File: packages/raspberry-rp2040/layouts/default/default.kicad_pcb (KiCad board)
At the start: 4 copper layers, 28 parts

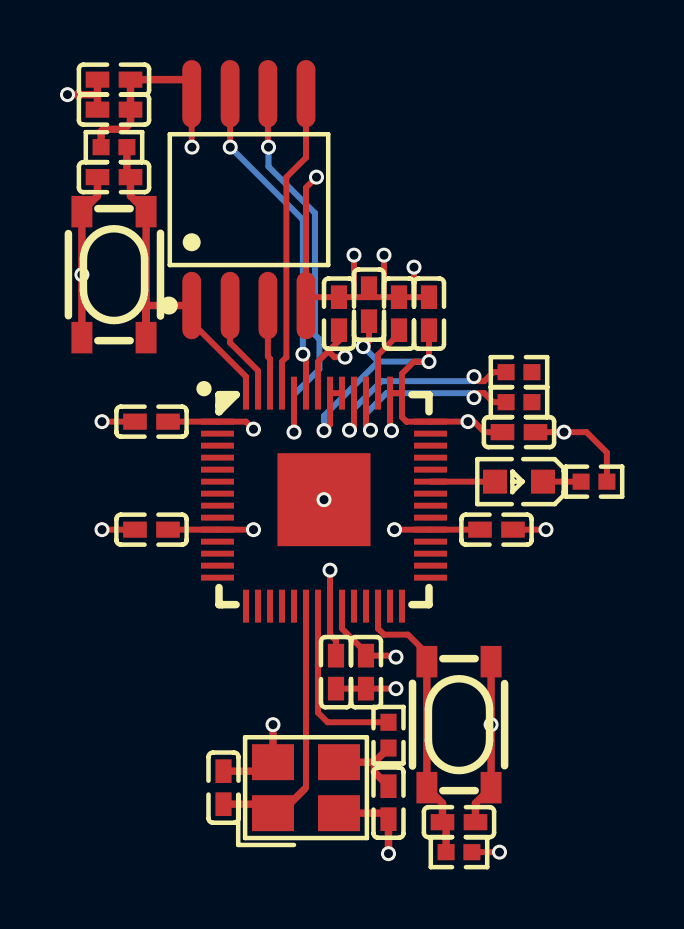
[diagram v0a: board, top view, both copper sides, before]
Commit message: fix docstrings, rename example > usage
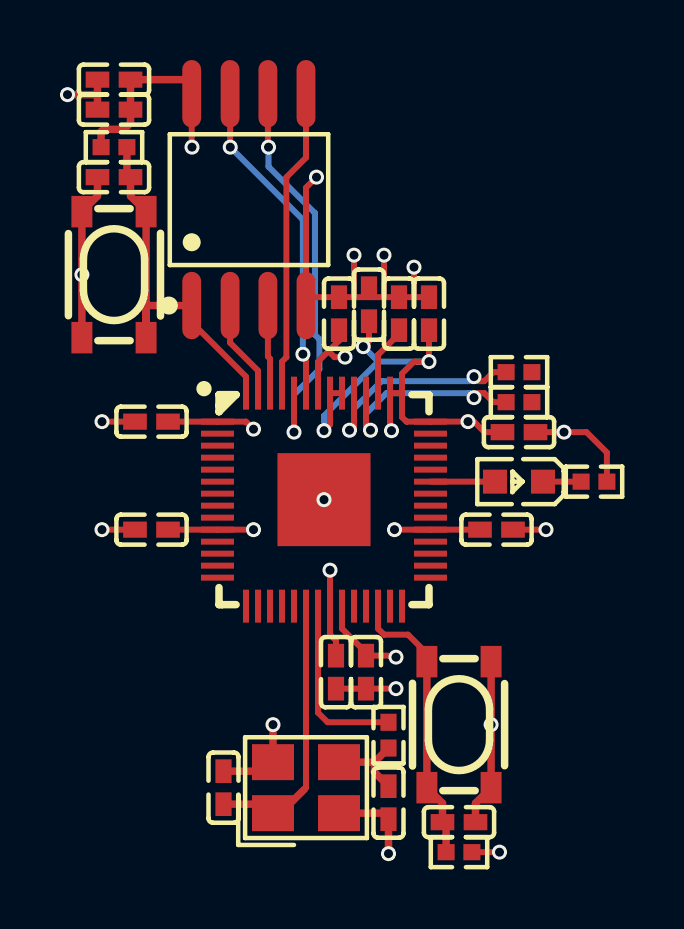
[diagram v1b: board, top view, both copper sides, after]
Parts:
- C5, C6: footprint YAGEO_CC0402JRNPO9BN150:C0402 -> FH_0402CG150J500NT:C0402
- R5, R6: footprint YAGEO_RC0402FR_0727RL:R0402 -> UNI_ROYAL_0402WGF270JTCE:R0402

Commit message: update regulator dependency
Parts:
- R5, R6: footprint UNI_ROYAL_0402WGF270JTCE:R0402 -> YAGEO_RC0402FR_0727RL:R0402
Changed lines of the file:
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@@
         )
     )
-    (footprint "UNI_ROYAL_0402WGF270JTCE:R0402"
+    (footprint "YAGEO_RC0402FR_0727RL:R0402"
         (layer "F.Cu")
         (at 6.5 -4.25 180)
@@
             )
         )
-        (property "Datasheet" "https://www.lcsc.com/datasheet/lcsc_datasheet_2205311900_UNI-ROYAL-Uniroyal-Elec-0402WGF270JTCE_C25100.pdf"
+        (property "Datasheet" "https://www.lcsc.com/datasheet/lcsc_datasheet_2304140030_YAGEO-RC0402FR-0727RL_C138021.pdf"
             (at 0 0 0)
             (layer "User.9")
@@
             )
         )
-        (property "checksum" "f5688ad61e98ad9a0b11cf3927eeb041cb72238f21c6b37db6cf4fe631cbd23f"
+        (property "checksum" "835ff2262c0c781dd32e754197fe87f02981eb4bce2fd6a49a20fee081a98441"
             (at 0 0 0)
             (layer "User.9")
@@
             )
         )
-        (property "__atopile_lib_fp_hash__" "3950a241-3b4c-5b6c-8f80-3fc849177d89"
+        (property "__atopile_lib_fp_hash__" "eb411b3a-b808-da41-e3c1-b5f79249ece2"
             (at 0 0 0)
             (layer "User.9")
@@
             )
         )
-        (property "LCSC" "C25100"
+        (property "LCSC" "C138021"
             (at 0 0 0)
             (layer "User.9")
@@
             )
         )
-        (property "Manufacturer" "UNI-ROYAL(Uniroyal Elec)"
+        (property "Manufacturer" "YAGEO"
             (at 0 0 0)
             (layer "User.9")
@@
             )
         )
-        (property "Partnumber" "0402WGF270JTCE"
+        (property "Partnumber" "RC0402FR-0727RL"
             (at 0 0 0)
             (layer "User.9")
@@
             (net 3 "USB_P")
         )
-        (model "${KIPRJMOD}/../../parts/UNI_ROYAL_0402WGF270JTCE/R0402_L1.0-W0.5-H0.4.step"
+        (model "${KIPRJMOD}/../../parts/YAGEO_RC0402FR_0727RL/R0402_L1.0-W0.5-H0.4.step"
             (offset
                 (xyz 0 0 0)
@@
         )
     )
-    (footprint "UNI_ROYAL_0402WGF270JTCE:R0402"
+    (footprint "YAGEO_RC0402FR_0727RL:R0402"
         (layer "F.Cu")
         (at 6.5 -3.25 180)
@@
             )
         )
-        (property "Datasheet" "https://www.lcsc.com/datasheet/lcsc_datasheet_2205311900_UNI-ROYAL-Uniroyal-Elec-0402WGF270JTCE_C25100.pdf"
+        (property "Datasheet" "https://www.lcsc.com/datasheet/lcsc_datasheet_2304140030_YAGEO-RC0402FR-0727RL_C138021.pdf"
             (at 0 0 0)
             (layer "User.9")
@@
             )
         )
-        (property "checksum" "f5688ad61e98ad9a0b11cf3927eeb041cb72238f21c6b37db6cf4fe631cbd23f"
+        (property "checksum" "835ff2262c0c781dd32e754197fe87f02981eb4bce2fd6a49a20fee081a98441"
             (at 0 0 0)
             (layer "User.9")
@@
             )
         )
-        (property "__atopile_lib_fp_hash__" "3950a241-3b4c-5b6c-8f80-3fc849177d89"
+        (property "__atopile_lib_fp_hash__" "eb411b3a-b808-da41-e3c1-b5f79249ece2"
             (at 0 0 0)
             (layer "User.9")
@@
             )
         )
-        (property "LCSC" "C25100"
+        (property "LCSC" "C138021"
             (at 0 0 0)
             (layer "User.9")
@@
             )
         )
-        (property "Manufacturer" "UNI-ROYAL(Uniroyal Elec)"
+        (property "Manufacturer" "YAGEO"
             (at 0 0 0)
             (layer "User.9")
@@
             )
         )
-        (property "Partnumber" "0402WGF270JTCE"
+        (property "Partnumber" "RC0402FR-0727RL"
             (at 0 0 0)
             (layer "User.9")
@@
             (net 6 "USB_N")
         )
-        (model "${KIPRJMOD}/../../parts/UNI_ROYAL_0402WGF270JTCE/R0402_L1.0-W0.5-H0.4.step"
+        (model "${KIPRJMOD}/../../parts/YAGEO_RC0402FR_0727RL/R0402_L1.0-W0.5-H0.4.step"
             (offset
                 (xyz 0 0 0)

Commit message: RP2040: Bump version (#104)
* Update ato.yaml

* experimental setup-atopile action

* revert

* rebuild layout

* update usage

* build with keep picked parts

---------

Co-authored-by: Sam Mellor <sam@atopile.io>
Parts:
- R5, R6: footprint YAGEO_RC0402FR_0727RL:R0402 -> UNI_ROYAL_0402WGF270JTCE:R0402

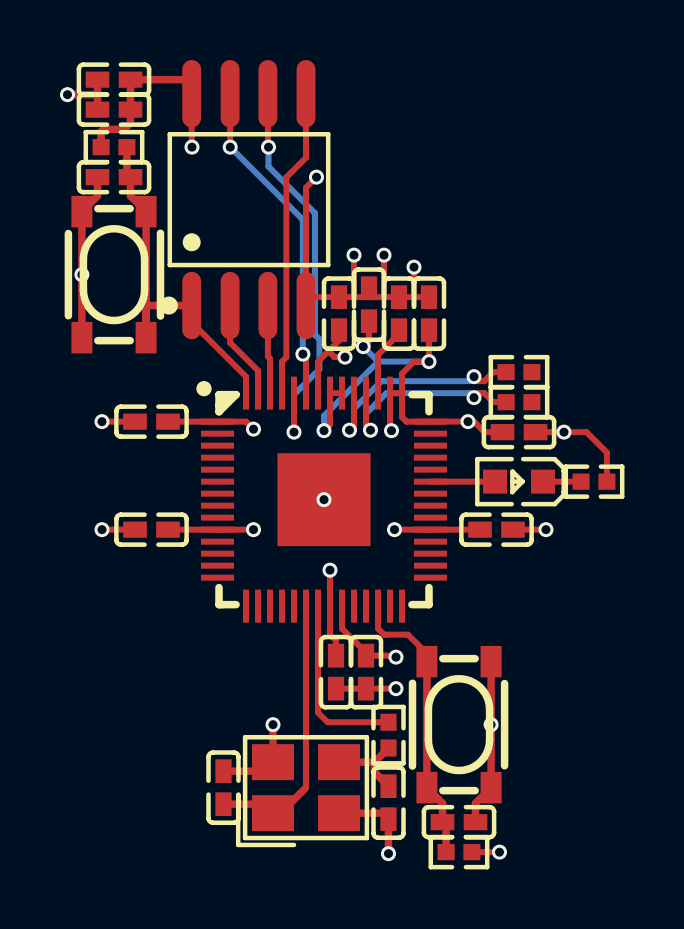
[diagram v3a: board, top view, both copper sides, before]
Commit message: Fix: RP2040: Factory enable missing connection (#108)
* Fix factory enable missing connection

* layout: add small power trace

* Add required mark for power
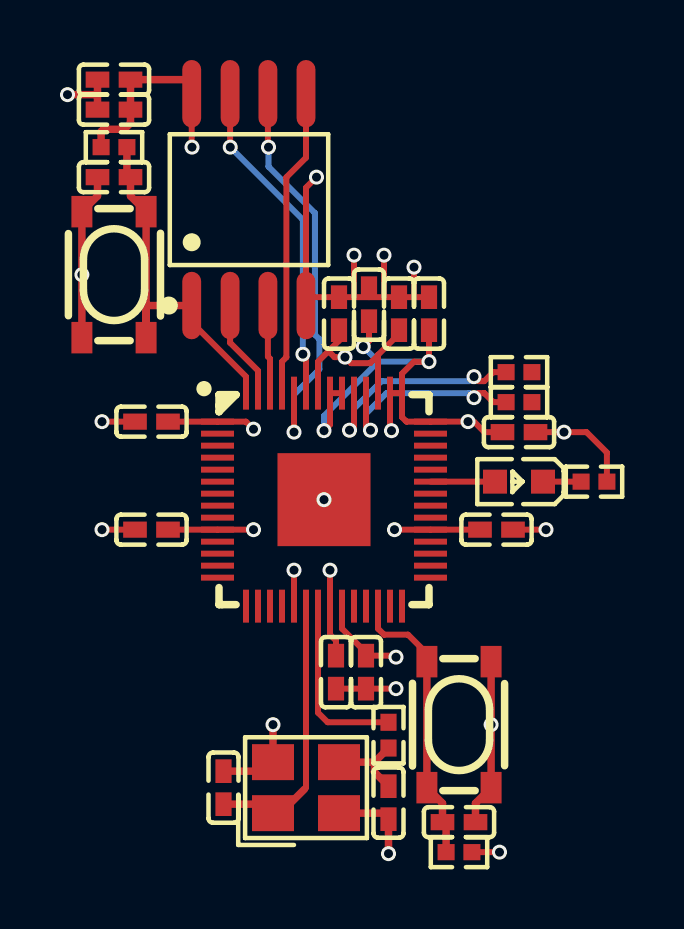
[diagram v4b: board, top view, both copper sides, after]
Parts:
- R5, R6: footprint UNI_ROYAL_0402WGF270JTCE:R0402 -> YAGEO_RC0402FR_0727RL:R0402
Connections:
- U1 pad 19: TESTEN -> gnd
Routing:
- net DVDD: track 8.41 -> 9.72 mm
- net gnd: track 40.6 -> 41.8 mm, vias 15 -> 16

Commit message: raspberry-rp2040: Use recommended crystal (#161)
Use the crystal recommended by Raspberry in their hardware design guide (ABM8-272-T3)
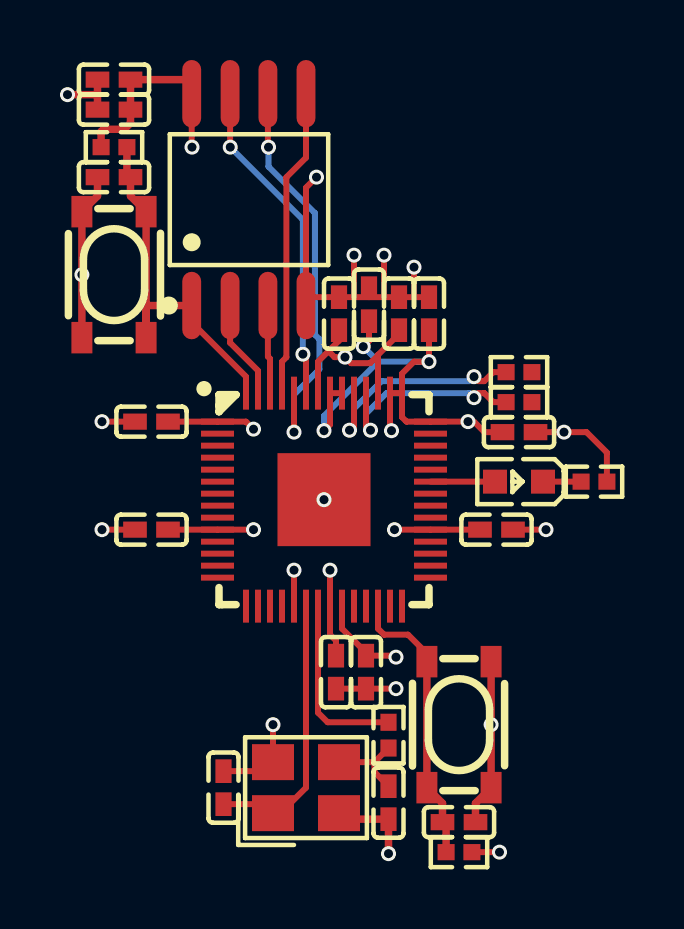
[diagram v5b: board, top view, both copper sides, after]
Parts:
- X1: footprint Yangxing_Tech_X322512MSB4SI:CRYSTAL-SMD_4P-L3.2-W2.5-BL -> Abracon_LLC_ABM8_272_T3:CRYSTAL-SMD_4P-L3.2-W2.5-BL
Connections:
- net -line-0 renamed gpio[26]-line
- net -line-1 renamed gpio[27]-line
- net -line-10 renamed SCL
- net -line-2 renamed gpio[28]-line
- net -line-3 renamed gpio[29]-line
- net -line-4 renamed TX
- net -line-5 renamed SCLK
- net -line-6 renamed MOSI
- net -line-7 renamed RX
- net -line-8 renamed MISO
- net -line-9 renamed SDA
- net DI renamed data_0
- net DO renamed data_1
- net DVDD renamed VCC
- net QSPI_SCLK renamed clock
- net QSPI_SD2 renamed data_2
- net QSPI_SD3 renamed data_3
- net QSPI_SS renamed chip_select
- net SWCLK renamed SWD_CLK
- net SWD renamed SWD_DIO
- net gnd renamed GND
- net xin renamed XIN
- net xout renamed XOUT

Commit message: Raspberry-RP2040: Remove debounce caps, custom net names, buttons dep. (#165)
* Remove debounce caps, custom net names, buttons dep.

* Remove old import
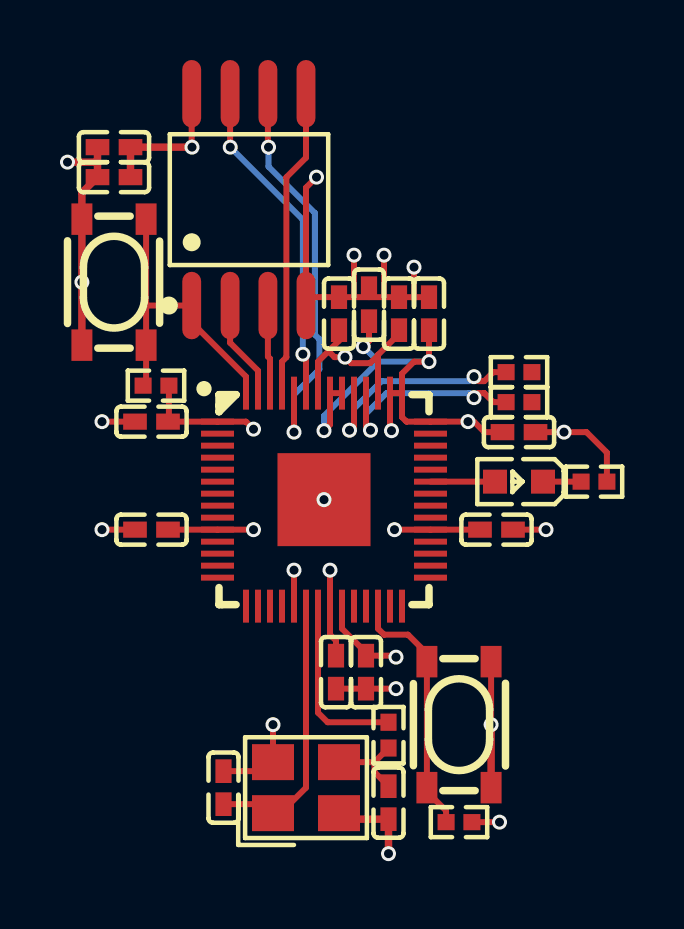
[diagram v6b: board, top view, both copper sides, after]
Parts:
- removed C1, C7: 1µF ±10% 25V X5R, Samsung_Electro_Mechanics_CL05A105KA5NQNC:C0402
- moved R1 8.07 mm to (-5.60, -3.80)
- moved C15 2.25 mm to (-7.00, -11.8)
- moved C16 2.25 mm to (-7.00, -10.8)
- moved R4 1.00 mm to (4.50, 10.8), turned to 0 degrees
- moved SW1 0.25 mm to (-7.00, -7.25), turned to -90 degrees
- turned SW2 to 90 degrees
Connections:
- net RP_USB_N renamed output-USB_D_N
- net RP_USB_P renamed output-USB_D_P
- net USB_N renamed input-USB_D_N
- net USB_P renamed input-USB_D_P
- net VCC renamed _core_regulator_out_power-VCC
- C10 pad 1: 3V3 -> power-VCC
- C11 pad 1: 3V3 -> power-VCC
- C12 pad 1: 3V3 -> power-VCC
- C13 pad 1: 3V3 -> power-VCC
- C14 pad 1: 3V3 -> power-VCC
- C15 pad 1: 3V3 -> power-VCC
- C16 pad 1: 3V3 -> power-VCC
- C8 pad 1: 3V3 -> power-VCC
- C9 pad 1: 3V3 -> power-VCC
- R1 pad 1: 3V3 -> chip_select
- R1 pad 2: chip_select -> power-VCC
- R4 pad 1: 3V3 -> RUN
- R4 pad 2: RUN -> power-VCC
- SW1 pad 1: GND -> chip_select
- SW1 pad 2: GND -> chip_select
- SW1 pad 3: chip_select -> GND
- SW1 pad 4: chip_select -> GND
- SW2 pad 1: GND -> RUN
- SW2 pad 2: GND -> RUN
- SW2 pad 3: RUN -> GND
- SW2 pad 4: RUN -> GND
- U1 pad 1: 3V3 -> power-VCC
- U1 pad 10: 3V3 -> power-VCC
- U1 pad 22: 3V3 -> power-VCC
- U1 pad 33: 3V3 -> power-VCC
- U1 pad 42: 3V3 -> power-VCC
- U1 pad 43: 3V3 -> power-VCC
- U1 pad 44: 3V3 -> power-VCC
- U1 pad 48: 3V3 -> power-VCC
- U1 pad 49: 3V3 -> power-VCC
- U2 pad 8: 3V3 -> power-VCC
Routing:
- net 3V3: track 36.8 -> 0.00 mm, vias 11 -> 0
- net power-VCC: track 0.00 -> 35.9 mm, vias 0 -> 11
- net chip_select: track 12.9 -> 10.8 mm
- net GND: track 41.8 -> 40.7 mm
- net RUN: track 9.61 -> 8.61 mm

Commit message: waiting on st-ldk220 to build for usage
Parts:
- C10, C11, C12, C13, C14, C16, C3, C4, C9: value 100nF ±10% 16V X7R -> 0F
- C15, C2, C8: value 2.2µF ±20% 6.3V X5R -> 0F
- C5, C6: value 15pF ±5% 50V C0G -> 0F
- R1, R3, R4: value 10kΩ ±1% 62.5mW -> 10000Ω
- R2: value 1kΩ ±1% 62.5mW -> 1000Ω
- R5, R6: value 27Ω ±1% 62.5mW -> 27Ω; footprint YAGEO_RC0402FR_0727RL:R0402 -> UNI_ROYAL_0402WGF270JTCE:R0402
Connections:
- net GPIO10 renamed 13
- net GPIO11 renamed 14
- net GPIO12 renamed 15
- net GPIO13 renamed 16
- net GPIO14 renamed 17
- net GPIO15 renamed 18
- net GPIO16 renamed 27
- net GPIO17 renamed 28
- net GPIO21 renamed 32
- net GPIO22 renamed 34
- net GPIO23 renamed 35
- net GPIO24 renamed 36
- net GPIO4 renamed 6
- net GPIO5 renamed 7
- net GPIO6 renamed 8
- net GPIO7 renamed 9
- net GPIO8 renamed 11
- net GPIO9 renamed 12
- net SWD_CLK renamed CLK
- net SWD_DIO renamed DIO
- net _core_regulator_out_power-VCC renamed core_power_decoupling_capacitor[2]-power-hv
- net chip_select renamed CHIP_SELECT
- net clock renamed CLOCK
- net data_0 renamed DATA_0
- net data_1 renamed DATA_1
- net data_2 renamed DATA_2
- net data_3 renamed DATA_3
- net gpio[26]-line renamed line
- net input-USB_D_N renamed input-DATA_N
- net input-USB_D_P renamed input-DATA_P
- net output renamed compensation_capacitors[1]-power-hv
- net output-USB_D_N renamed DATA_N
- net output-USB_D_P renamed DATA_P
- net power-VCC renamed hv
- C10 pad 2: GND -> lv
- C11 pad 2: GND -> lv
- C12 pad 2: GND -> lv
- C13 pad 2: GND -> lv
- C14 pad 2: GND -> lv
- C15 pad 2: GND -> lv
- C16 pad 2: GND -> lv
- C2 pad 2: GND -> power-lv
- C3 pad 2: GND -> power-lv
- C4 pad 2: GND -> power-lv
- C5 pad 2: GND -> power-lv
- C6 pad 2: GND -> power-lv
- C8 pad 2: GND -> lv
- C9 pad 2: GND -> lv
- R3 pad 1: GND -> lv
- SW1 pad 3: GND -> lv
- SW1 pad 4: GND -> lv
- SW2 pad 3: GND -> lv
- SW2 pad 4: GND -> lv
- U1 pad 19: GND -> lv
- U1 pad 57: GND -> lv
- U2 pad 4: GND -> lv
- X1 pad 2: GND -> power-lv
- X1 pad 4: GND -> power-lv
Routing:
- net GND: track 40.7 -> 0.00 mm, vias 16 -> 0
- net 46: track 0.00 -> 40.7 mm, vias 0 -> 16
- net hv: track 35.9 -> 0.00 mm, vias 11 -> 0
- net 39: track 0.00 -> 35.9 mm, vias 0 -> 11
- net core_power_decoupling_capacitor[2]-power-hv: track 9.72 -> 0.00 mm, vias 2 -> 0
- net 1: track 0.00 -> 9.72 mm, vias 0 -> 2
- net XIN: track 9.28 -> 0.00 mm
- net 24: track 0.00 -> 9.28 mm
- net compensation_capacitors[1]-power-hv: track 2.84 -> 0.00 mm
- net 45: track 0.00 -> 2.84 mm
